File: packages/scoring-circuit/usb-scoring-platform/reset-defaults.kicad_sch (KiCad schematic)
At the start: 27 parts

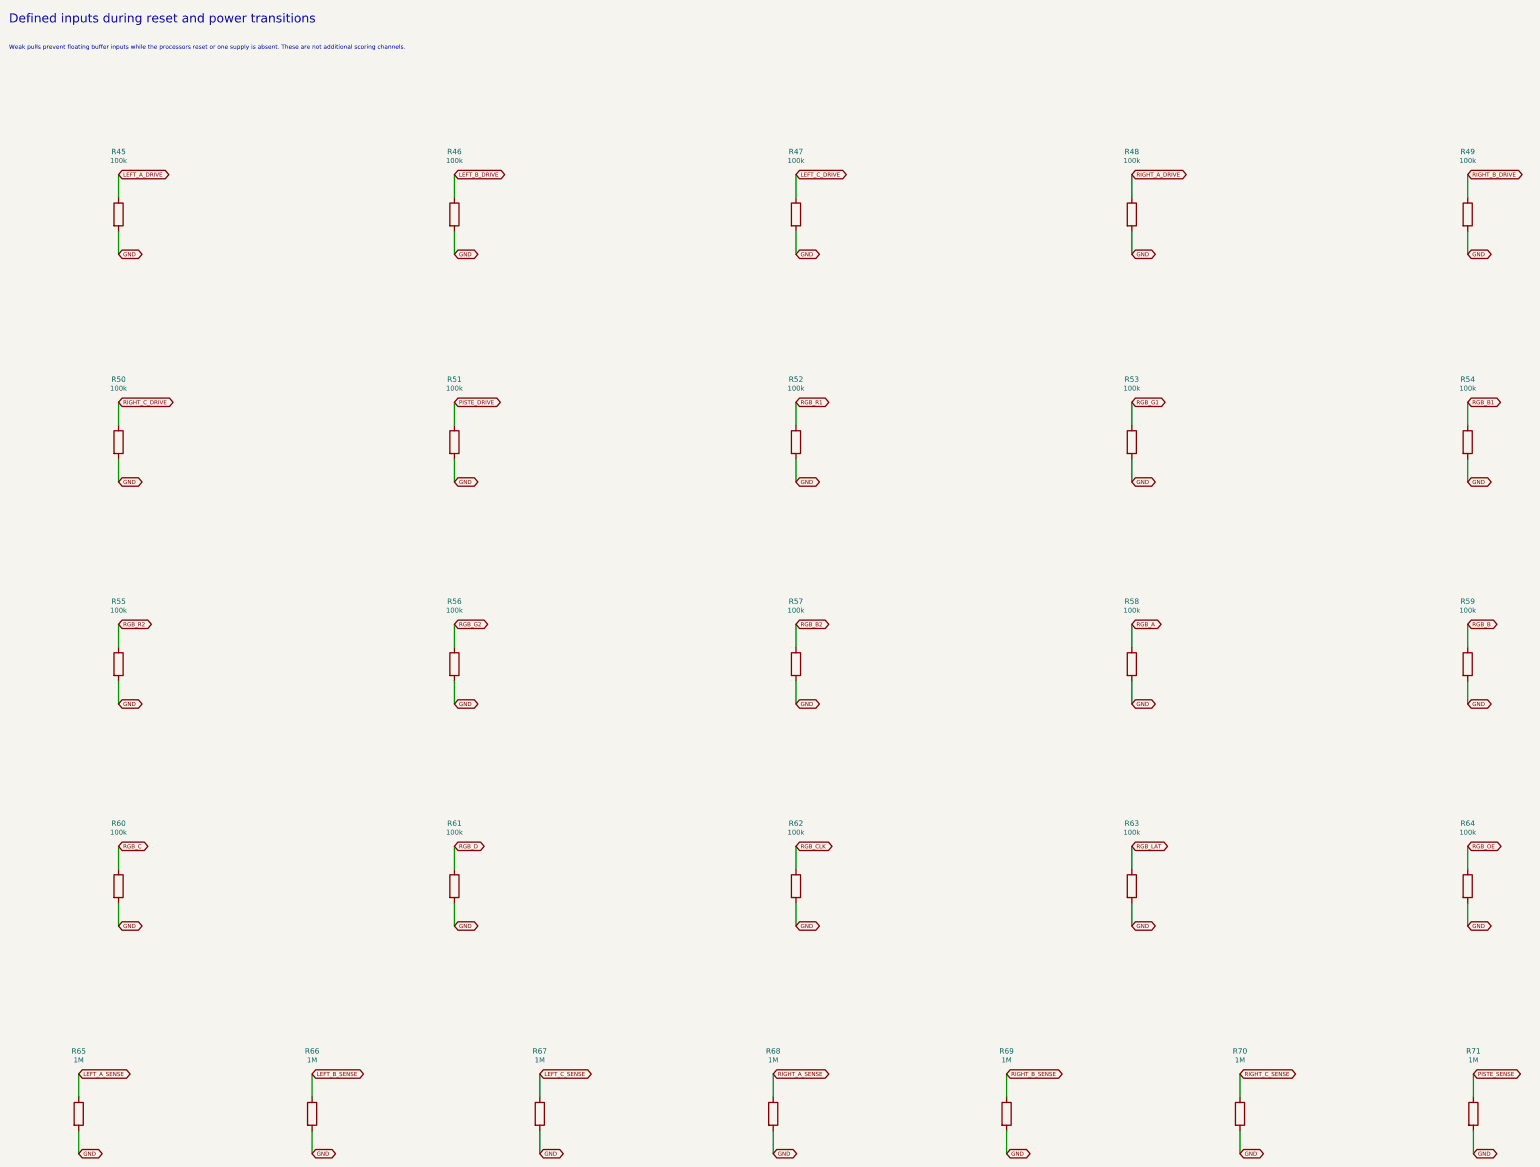
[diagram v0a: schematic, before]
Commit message: fix(scoring-circuit): strengthen STM32 sensing bias and model continuity
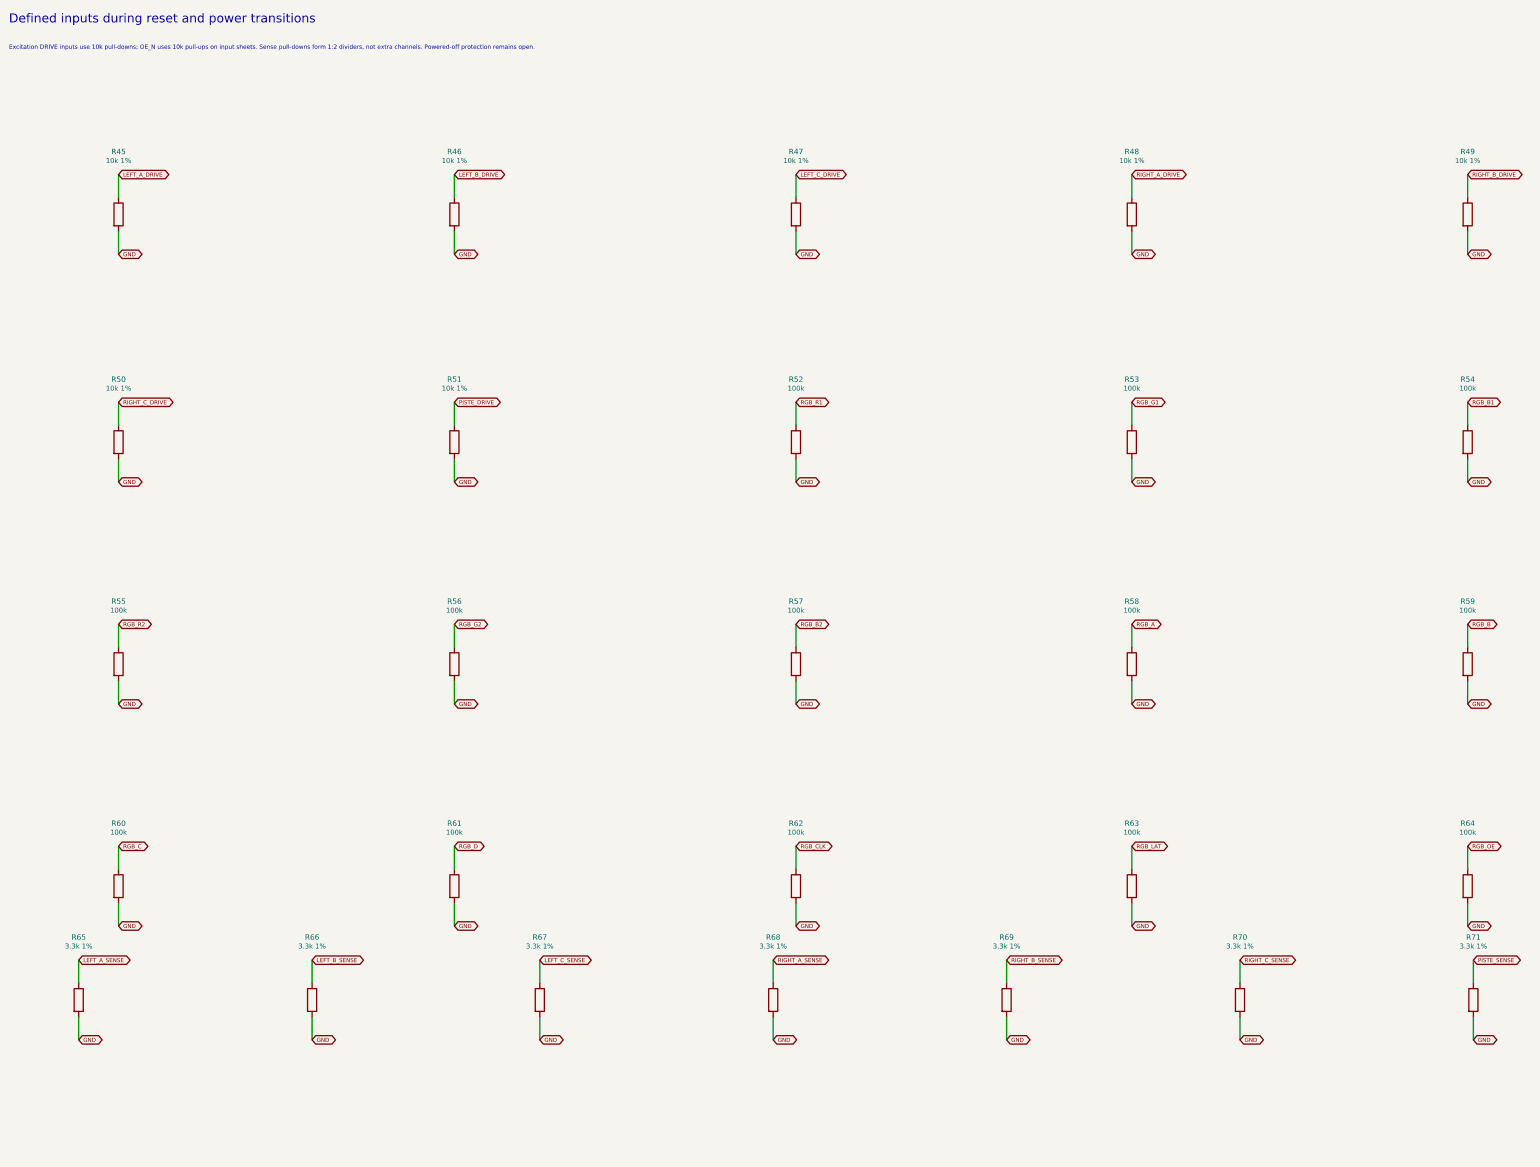
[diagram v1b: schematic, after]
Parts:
- R45, R46, R47, R48, R49, R50, R51: value 100k -> 10k 1%
- R65, R66, R67, R68, R69, R70, R71: value 1M -> 3.3k 1%
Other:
- note added: "Excitation DRIVE inputs use 10k pull-downs; OE_N uses 10k pull-ups on input sheets. Sense pull-downs form 1:2 dividers, not extra channels. Powered-off protection remains open."
- note removed: "Weak pulls prevent floating buffer inputs while the processors reset or one supply is absent. These are not additional scoring channels."
- moved on the sheet: R65, R66, R67, R68, R69, R70, R71

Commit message: refactor(scoring-circuit): remove redundant display pull-downs
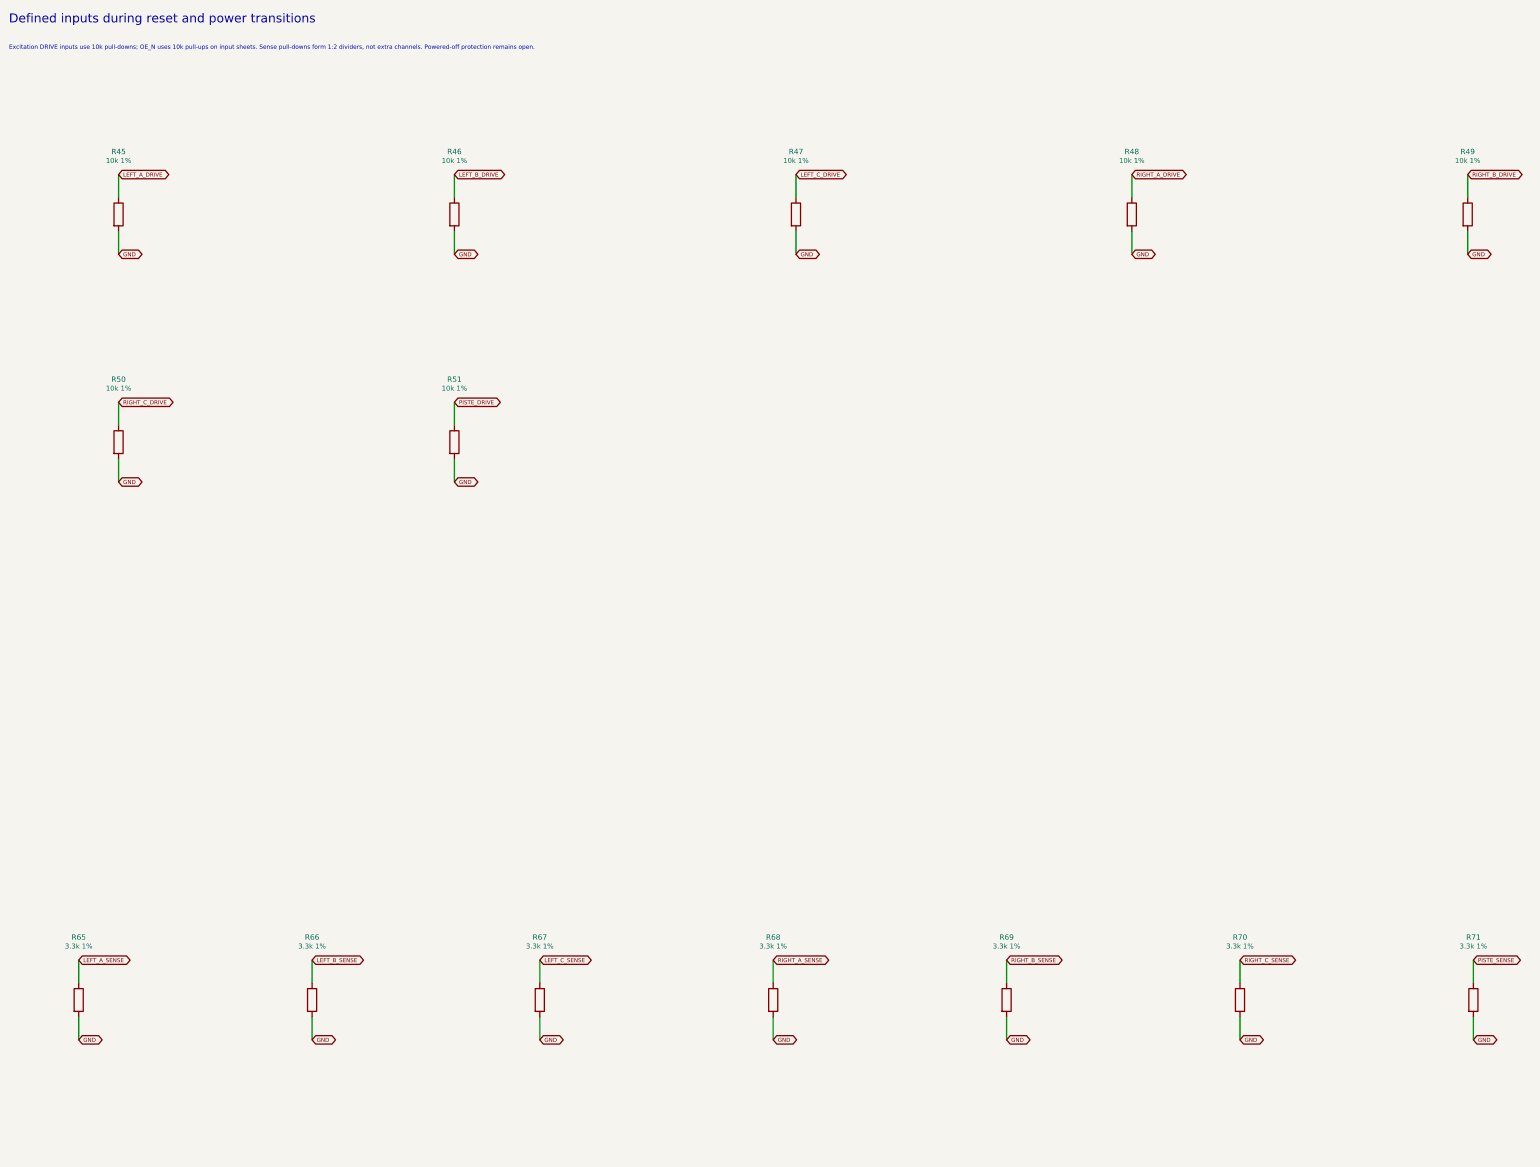
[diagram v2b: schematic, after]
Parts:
- removed R52, R53, R54, R55, R56, R57, R58, R59, R60, R61, R62, R63, R64: 100k, Resistor_SMD:R_0603_1608Metric, symbol Device:R

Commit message: feat(scoring-circuit): select exact prototype resistor parts
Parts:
- R45, R46, R47, R48, R49, R50, R51: MPN (none) -> RC0603FR-0710KL; Manufacturer (none) -> YAGEO
- R65, R66, R67, R68, R69, R70, R71: MPN (none) -> RC0603FR-073K3L; Manufacturer (none) -> YAGEO

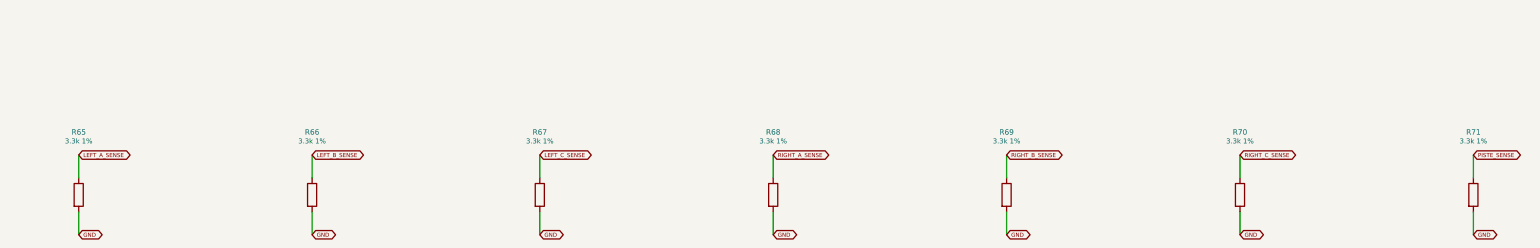
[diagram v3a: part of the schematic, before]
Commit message: fix(scoring): shorten acquisition scan and qualify contact inputs
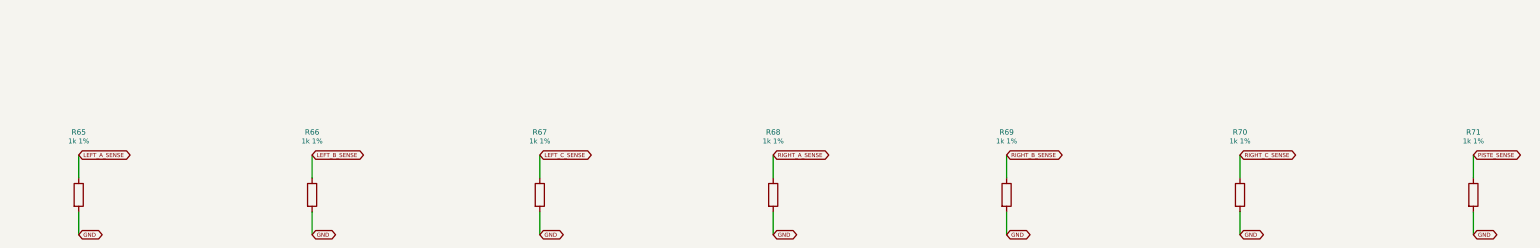
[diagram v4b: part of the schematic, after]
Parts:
- R65, R66, R67, R68, R69, R70, R71: value 3.3k 1% -> 1k 1%; MPN RC0603FR-073K3L -> RC0603FR-071KL
